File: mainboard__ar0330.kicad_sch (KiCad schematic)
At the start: 28 parts

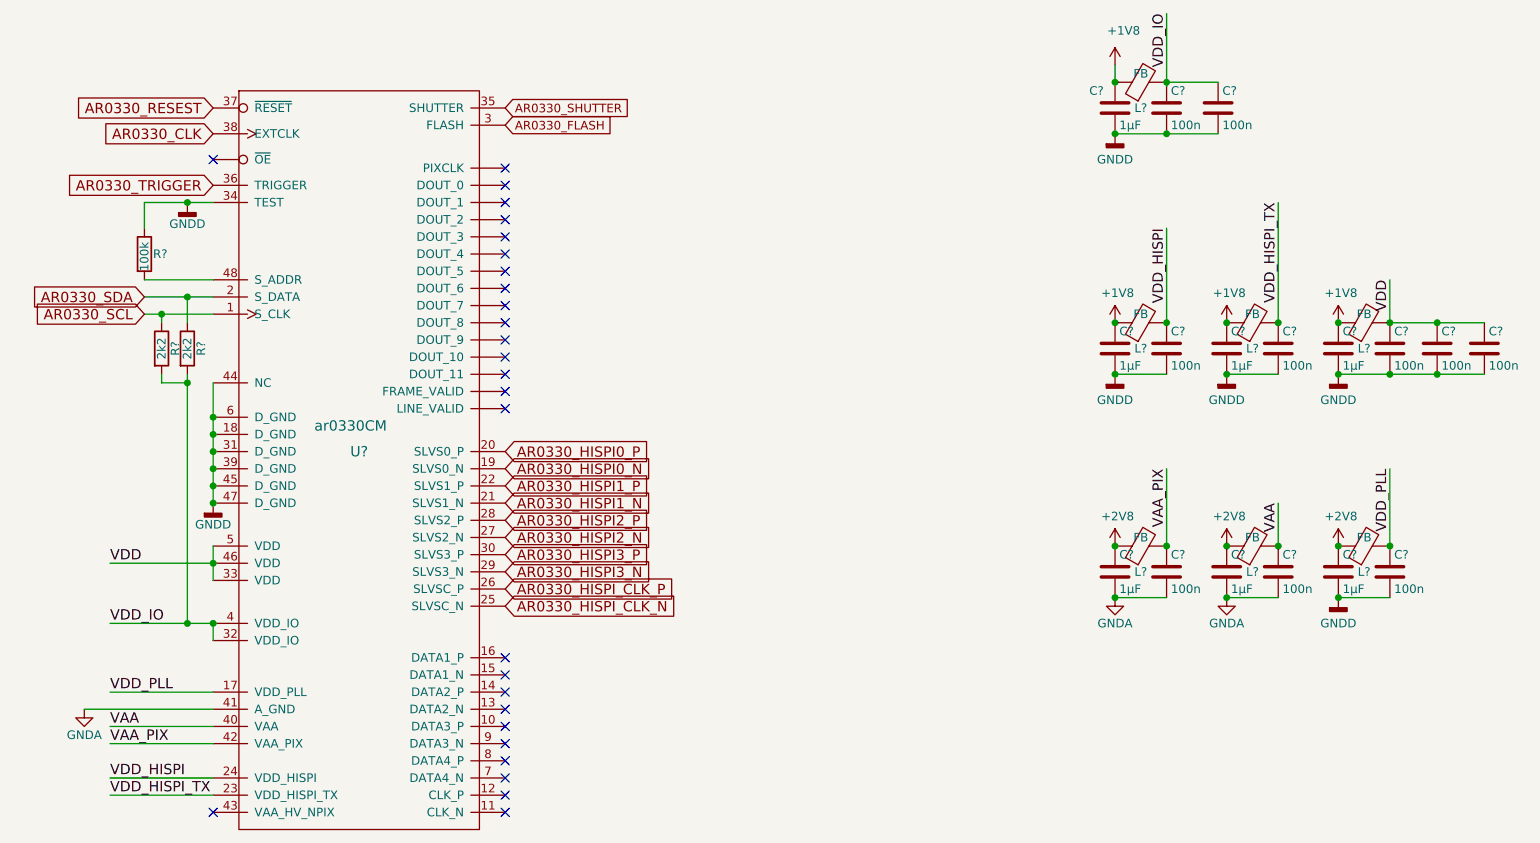
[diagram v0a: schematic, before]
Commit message: small tweaks; add mipi termination
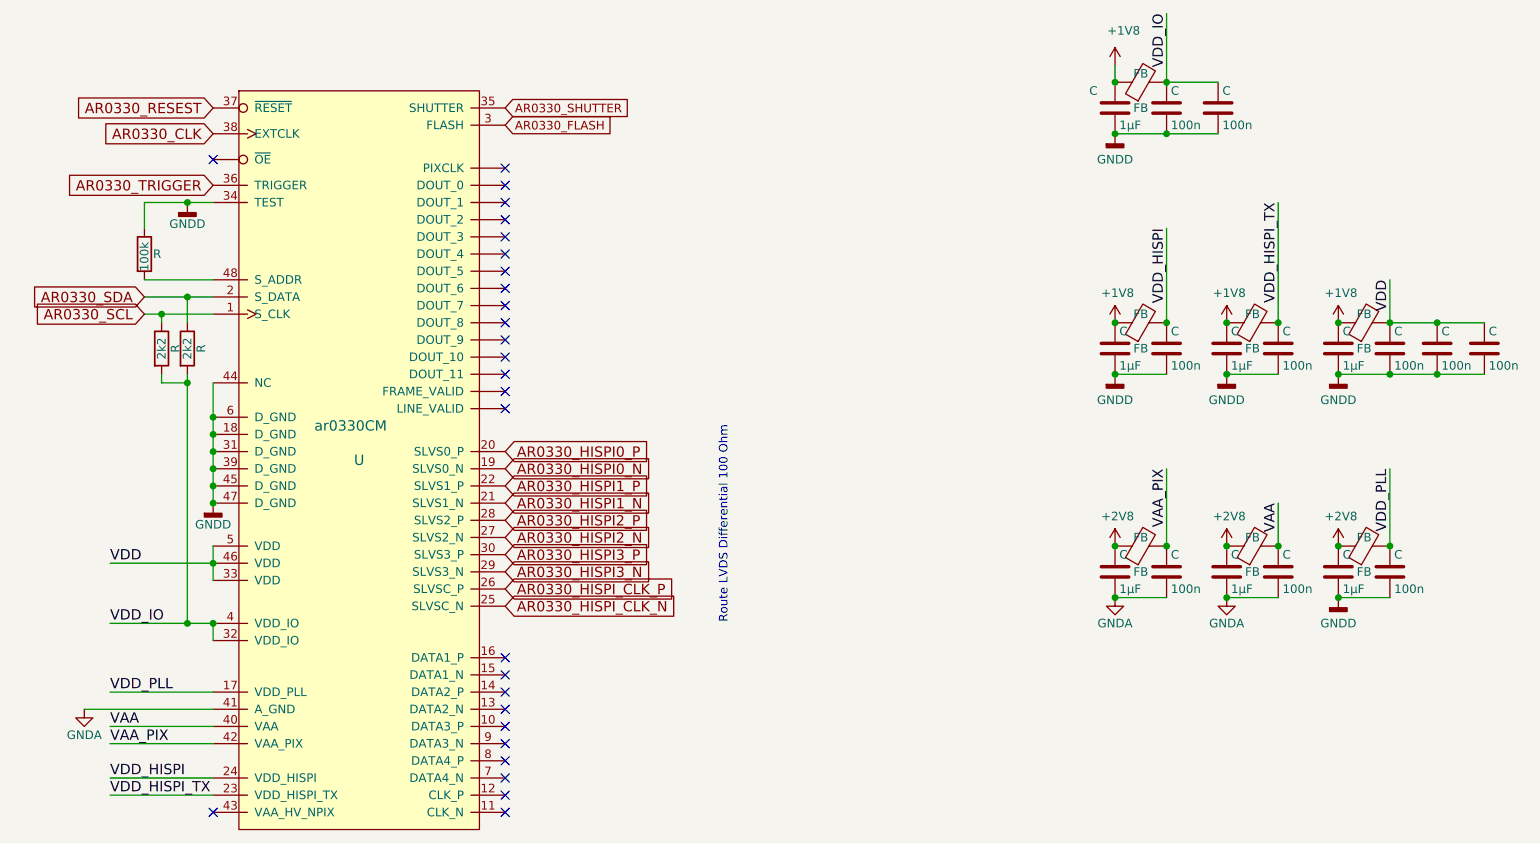
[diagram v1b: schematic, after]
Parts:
- U: renamed from U?; symbol ar0330cm:ar0330CM -> image_sensor:AR0330CM
- gave numbers to parts that had none: 3
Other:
- note added: "Route LVDS Differential 100 Ohm"
